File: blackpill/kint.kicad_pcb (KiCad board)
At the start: 2 copper layers, 99.9 x 86 mm, 21 parts, among them J1 THUMB_RIGHT_SPC_KB600, J2 LEFT_13_LT, J3 TOP_LEFT, J4 TOP_RIGHT, J5 THUMB_LEFT_BAK, J6 THUMB_RIGHT_SPC, J7 RIGHT_13_DOWN, J8 THUMB_LEFT_BAK_KB600, U1 YAAJ_WeAct_BlackPill_Part_Lik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

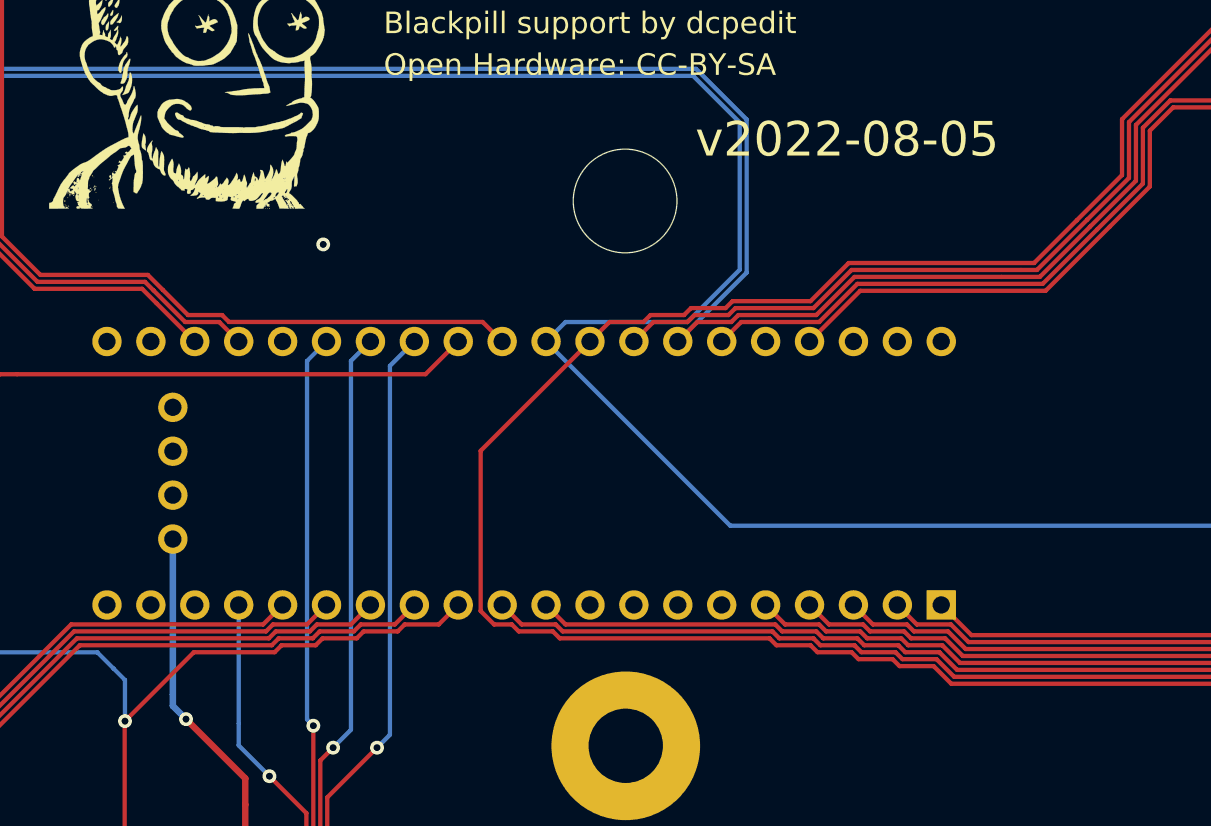
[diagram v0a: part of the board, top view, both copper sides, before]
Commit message: Update to remove the need to connect center pins
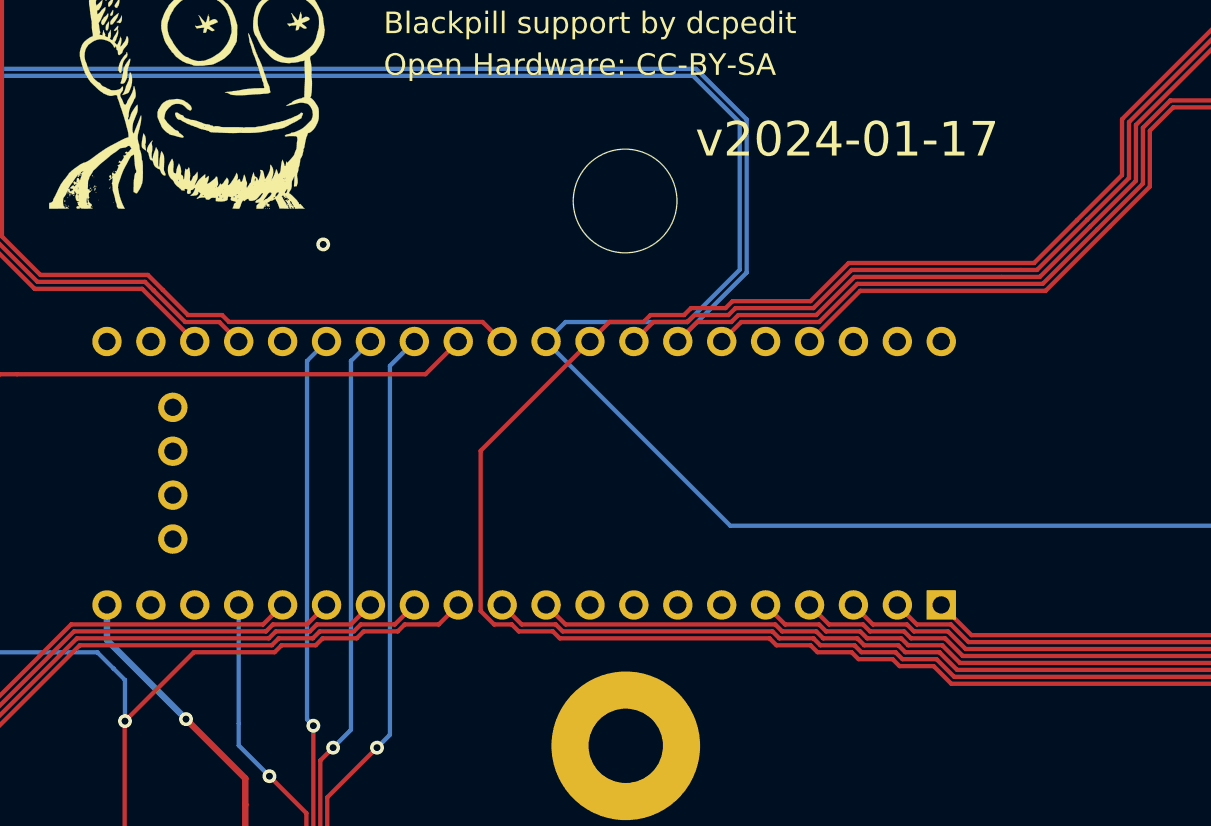
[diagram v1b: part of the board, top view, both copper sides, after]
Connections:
- U1 pad 20: unconnected-(U1-Pad20) -> /3V3
- U1 pad 44: /3V3 -> unconnected-(U1-3V3-Pad44)
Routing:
- net /3V3: track 77.0 -> 74.8 mm
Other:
- board text added: "v2024-01-17"
- board text removed: "v2022-08-05"
